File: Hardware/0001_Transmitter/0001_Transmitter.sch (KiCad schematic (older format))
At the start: 0 parts

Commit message: fix 0001_Transmitter directories
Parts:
- added AE?: Antenna, symbol Device:Antenna
- added C1, C? (x5): 1u, symbol 0001_Transmitter:C
- added C10: 15n, symbol 0001_Transmitter:C
- added C10: C, symbol 0001_Transmitter:C
- added C11, C6, C8, C? (x2): 0.1u, symbol 0001_Transmitter:C
- added C2, C4, C7: 10u, symbol 0001_Transmitter:C
- added C3: .01u, symbol 0001_Transmitter:C
- added C5: .47u, symbol 0001_Transmitter:C
- added C7: 1uF, symbol 0001_Transmitter:C
- added C9: 2.2n, symbol 0001_Transmitter:C
- added IN, OUT: 2510-6002UB, 3M_2510-6002UB, symbol 2510-6002UB:2510-6002UB
- added R?: 330, symbol 0001_Transmitter:R
- added R? (x9): R, symbol 0001_Transmitter:R
- added R?: 10, symbol 0001_Transmitter:R
- added U?: Teensy4.0, symbol teensy:Teensy4.0
- added U?: LMX2572, symbol 0001_Transmitter-cache:LMX2572
- added U?: ASDMB-100.000MHZ-LY-T, symbol 0001_Transmitter:ASDMB-100.000MHZ-LY-T
- added U?: SN65HVD230, Package_SO:SOIC-8_3.9x4.9mm_P1.27mm, symbol Interface_CAN_LIN:SN65HVD230
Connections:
- net labels added: CANH, CANL, CAN_RX, CAN_TX, CS, GND, MISO, MOSI, RAMPCLK, RAMPDIR, SCK, SYNC, SYSREFREQ, VDC_3V3
- wire segments 0 -> 120
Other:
- note added: "SPACESHOT RF SCHEMATIC I"

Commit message: fixed a bunch of the library stuff (hopefully)
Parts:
- removed AE?: Antenna, symbol Device:Antenna
- removed U?: Teensy4.0, symbol teensy:Teensy4.0
- added U?: Teensy4.0, symbol teensy:Teensy4.0
- U?: symbol 0001_Transmitter-cache:LMX2572 -> schematic_1:LMX2572-0001_Transmitter-cache
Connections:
- wire segments 120 -> 138

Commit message: fixed some more stuff, needs to be double checked & prettified
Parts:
- removed IN, OUT: 2510-6002UB, 3M_2510-6002UB, symbol 2510-6002UB:2510-6002UB
- removed R? (x4): R, symbol 0001_Transmitter:R
- removed U?: LMX2572, symbol schematic_1:LMX2572-0001_Transmitter-cache
- added C?: 100nF, symbol 0001_Transmitter:C
- added P? (x2): CONN_5x2, symbol 0001_Transmitter:CONN_5x2
- added R?: 10, symbol 0001_Transmitter:R
- added R? (x2): R, symbol 0001_Transmitter:R
- added U?: LMX2594RHAT, symbol 0001_Transmitter:LMX2594RHAT
- C14: renamed from C8; value 0.1u -> 100nF
- C16: renamed from C11; value 0.1u -> 100pF
- C17: renamed from C?; value 0.1u -> 100pF
- U?: symbol Interface_CAN_LIN:SN65HVD230 -> schematic_1:SN65HVD230-Interface_CAN_LIN
- gave numbers to parts that had none: 15
- renumbered C6 to C10, C7 to C13, C9 to C18, C10 to C19, C7 to C2, C10 to C20, C2 to C3, C3 to C4, C4 to C5, C5 to C8
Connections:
- net labels added: SYSREQREF
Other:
- note removed: "SPACESHOT RF SCHEMATIC I"
- moved on the sheet: C1, C10, C11, C12, C13, C14, C15, C16, C17, C18, C19, C2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

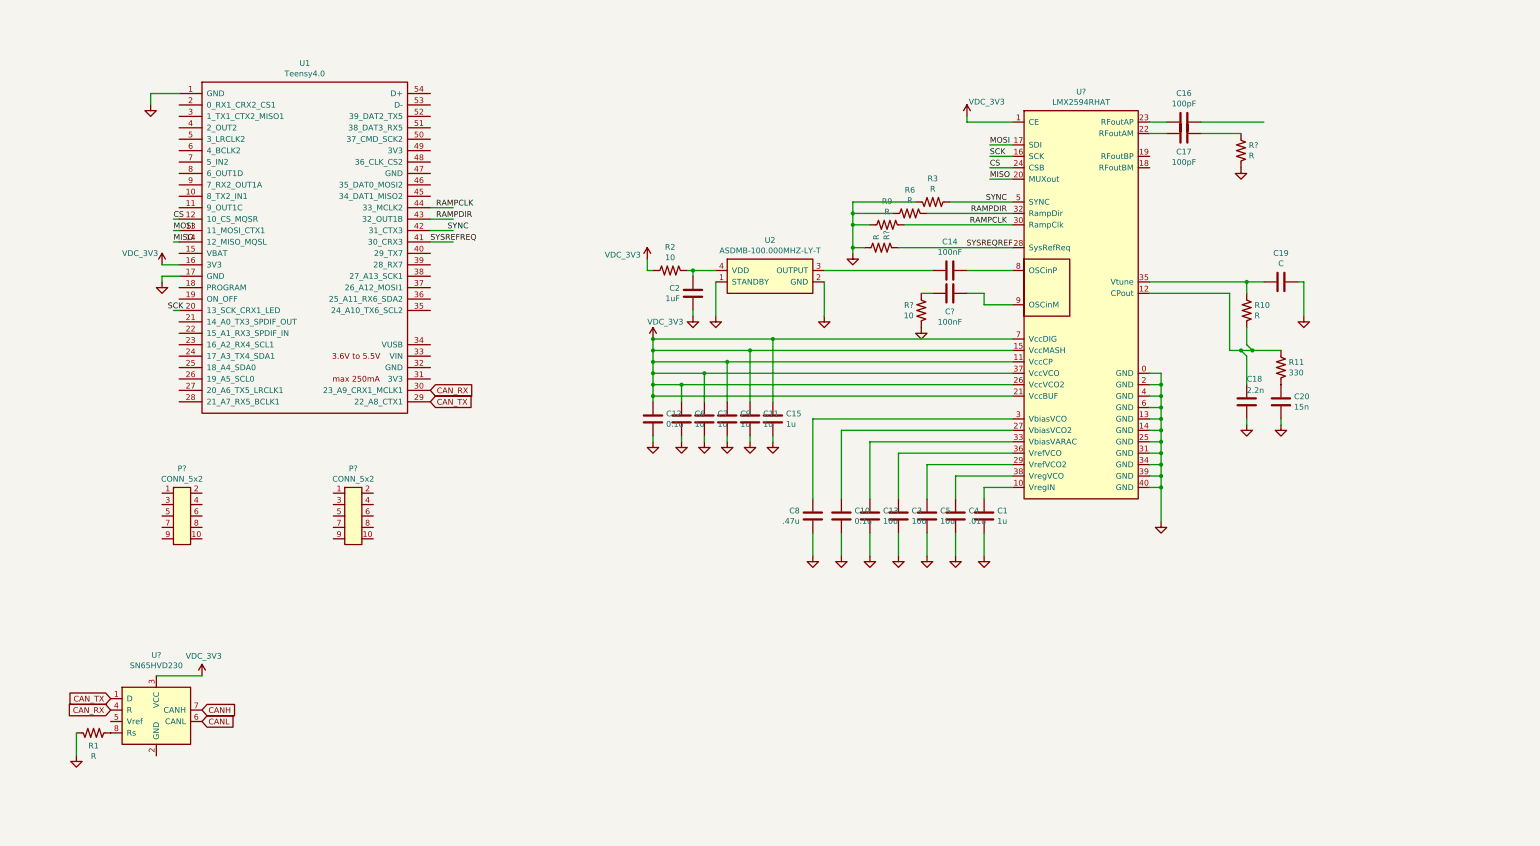
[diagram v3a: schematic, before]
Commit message: verified some cap values, moved some stuff around to make it look better
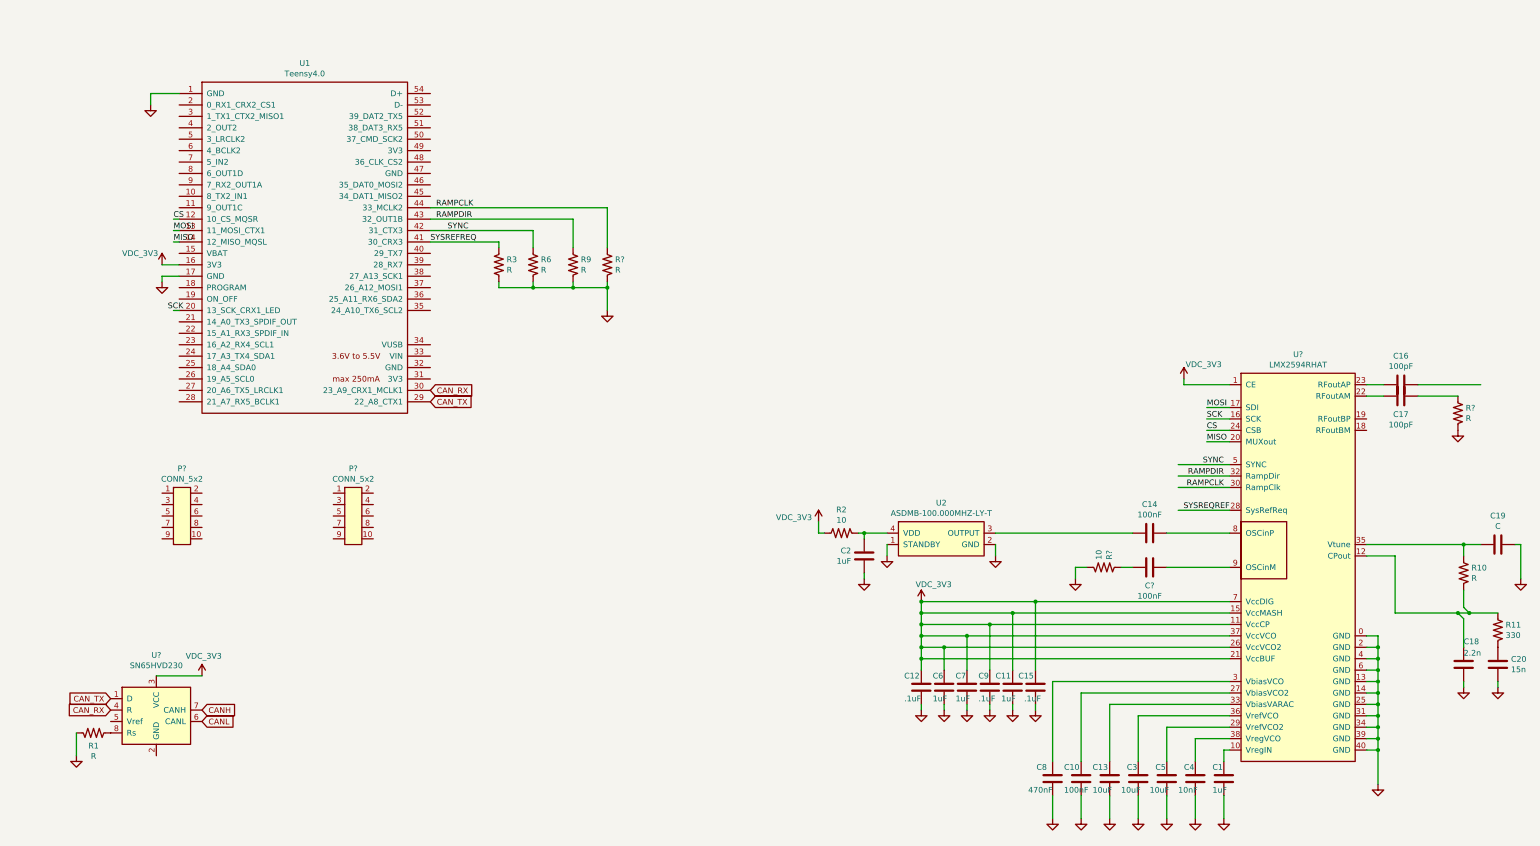
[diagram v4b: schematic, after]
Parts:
- C1, C11, C6, C7: value 1u -> 1uF
- C10: value 0.1u -> 100nF
- C12: value 0.1u -> .1uF
- C13, C3, C5: value 10u -> 10uF
- C15, C9: value 1u -> .1uF
- C4: value .01u -> 10nF
- C8: value .47u -> 470nF
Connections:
- wire segments 138 -> 142
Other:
- moved on the sheet: C1, C10, C11, C12, C13, C14, C15, C16, C17, C18, C19, C2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
